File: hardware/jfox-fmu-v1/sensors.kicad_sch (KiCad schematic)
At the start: 5 parts, among them U1 ICM-42688-P, U2 ICM-45686, U3 BMI088, U4 BMP388, U5 FM25V02A

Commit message: Footprint every part, and verify each one exists
58 of 58 components now carry a footprint chosen against the package its
datasheet specifies, and check_fmu_footprints.py confirms every name resolves
to a file on disk.

Three of the names this design was carrying did not. The symbol library named
`Sensor_Motion:InvenSense_QFN-14_3x3mm_P0.5mm` and
`Sensor_Pressure:Bosch_LGA-10_2x2mm_P0.35mm`, neither of which is a footprint
in any installed library - both plausible, both fiction. The third was worse:
`Package_LGA:Bosch_LGA-14_3x2.5mm_P0.5mm` is real, matches the InvenSense
package on every word of its name, and is drawn for the BMI160 with 0.675 mm
pads where InvenSense wants 0.475 mm.

Notable choices, each traceable:
  LTC4417CGN  GN is the 16-lead narrow SSOP.
  TPS62132    RGT 3x3 VQFN. TI's land drawing (4222419/E) gives the exposed
              pad as 1.55 mm; KiCad's 1.6 mm variant is closest. Thermal-via
              variant, since the datasheet is explicit that the pad must be
              soldered and that dissipation limits output power.
  Bulk caps   4u7/10u/22u get an 0805, not the 0402 every other capacitor
              gets. Assigning one size to all of them produces a board that
              cannot be built from the BOM it ships with.
  L1          a generic 1210 land, and labelled as such - the 2.2 uH part is
              not chosen yet, since saturation current and DCR still have to
              be picked against the real 550 mA peak.

The checker was wrong on its first run, in a way worth recording because the
failure mode is self-concealing. It matched ref, value and footprint in one
regex with the footprint group optional, so a component with no footprint -
precisely what it exists to find - failed to match at all, dropped out of the
list, and the run reported "every component maps to a footprint" while the
count quietly fell by one. A check whose failure mode is to stop seeing the
failure is worse than no check. Now it splits into per-com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
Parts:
- U1, U2: footprint (none) -> jfox-fmu:InvenSense_LGA-14_2.5x3mm_P0.5mm
- U3: footprint (none) -> Package_LGA:Bosch_LGA-16_4.5x3mm_P0.5mm_LayoutBorder7x1y_ClockwisePinNumbering
- U4: footprint (none) -> jfox-fmu:Bosch_LGA-10_2x2mm_P0.5mm_LayoutBorder2x3y
- U5: footprint (none) -> Package_SO:SOIC-8_3.9x4.9mm_P1.27mm
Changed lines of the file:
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@@
+		)
+		)
+		(property "Footprint" "jfox-fmu:InvenSense_LGA-14_2.5x3mm_P0.5mm"
+			(at 66.04 59.69 0)
+			(hide yes)
+			(effects
+			(font
+				(size 1.27 1.27)
+			)
 		)
 		)
 		(instances
 			(project "jfox-fmu"
-				(path "/3f1d7739-de78-4a9b-8f02-2fa580b1af15"
+				(path "/fce3b1be-4717-4f75-b07b-c3376dbd2263"
 					(reference "U1")
 					(unit 1)
@@
 		)
 		)
+		(property "Footprint" "jfox-fmu:InvenSense_LGA-14_2.5x3mm_P0.5mm"
+			(at 154.94 59.69 0)
+			(hide yes)
+			(effects
+			(font
+				(size 1.27 1.27)
+			)
+		)
+		)
 		(instances
 			(project "jfox-fmu"
-				(path "/3f1d7739-de78-4a9b-8f02-2fa580b1af15"
+				(path "/fce3b1be-4717-4f75-b07b-c3376dbd2263"
 					(reference "U2")
 					(unit 1)
@@
 		)
 		)
+		(property "Footprint" "jfox-fmu:Bosch_LGA-10_2x2mm_P0.5mm_LayoutBorder2x3y"
+			(at 66.04 125.73 0)
+			(hide yes)
+			(effects
+			(font
+				(size 1.27 1.27)
+			)
+		)
+		)
 		(instances
 			(project "jfox-fmu"
-				(path "/3f1d7739-de78-4a9b-8f02-2fa580b1af15"
+				(path "/fce3b1be-4717-4f75-b07b-c3376dbd2263"
 					(reference "U4")
 					(unit 1)
@@
 		)
 		)
+		(property "Footprint" "Package_SO:SOIC-8_3.9x4.9mm_P1.27mm"
+			(at 154.94 125.73 0)
+			(hide yes)
+			(effects
+			(font
+				(size 1.27 1.27)
+			)
+		)
+		)
 		(instances
 			(project "jfox-fmu"
-				(path "/3f1d7739-de78-4a9b-8f02-2fa580b1af15"
+				(path "/fce3b1be-4717-4f75-b07b-c3376dbd2263"
 					(reference "U5")
 					(unit 1)
@@
 		)
 		)
+		(property "Footprint" "Package_LGA:Bosch_LGA-16_4.5x3mm_P0.5mm_LayoutBorder7x1y_ClockwisePinNumbering"
+			(at 66.04 191.77 0)
+			(hide yes)
+			(effects
+			(font
+				(size 1.27 1.27)
+			)
+		)
+		)
 		(instances
 			(project "jfox-fmu"
-				(path "/3f1d7739-de78-4a9b-8f02-2fa580b1af15"
+				(path "/fce3b1be-4717-4f75-b07b-c3376dbd2263"
 					(reference "U3")
 					(unit 1)

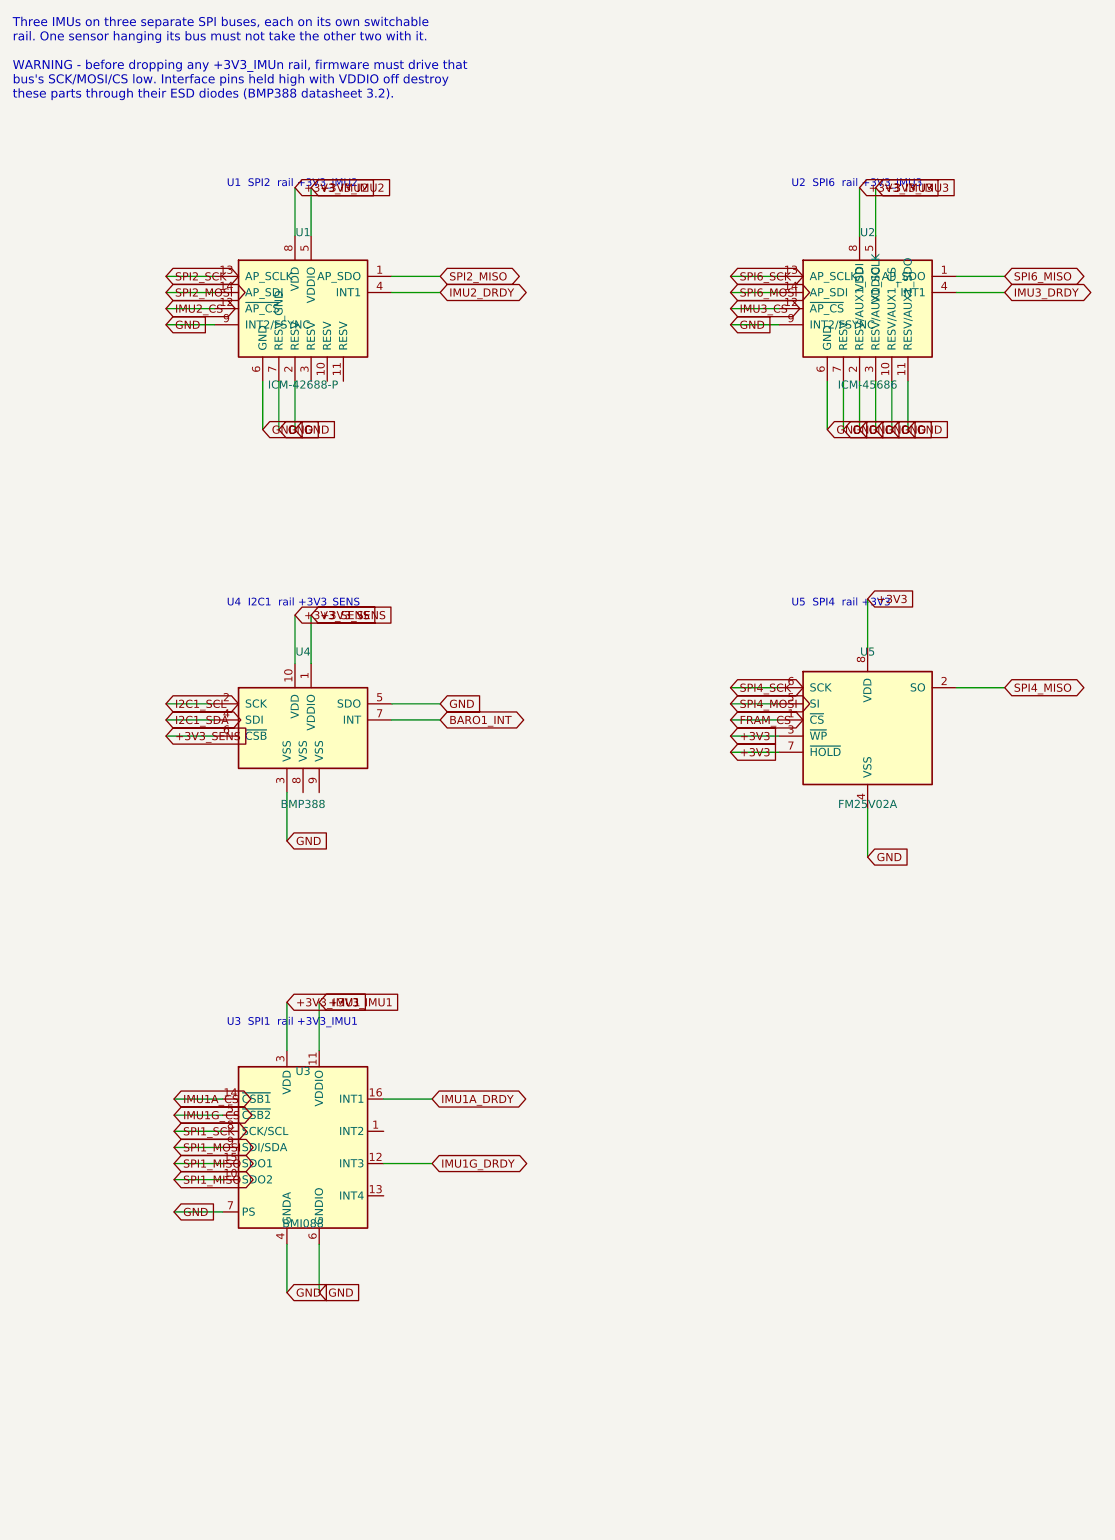
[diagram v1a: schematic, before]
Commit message: Add the two sensors the design said it had
ARCHITECTURE.md specifies two barometers from two vendors and an internal
magnetometer. The schematic had one barometer and no magnetometer, and had had
neither for the whole life of the board. Every check passed the entire time.

That is the interesting part. The datasheet checks ask "is this part wired the
way its datasheet says", and all of them can pass on a board that is wired
perfectly and is still the wrong board. The nets for the missing sensors
existed - MAG_DRDY and BARO2_INT, correctly named, allocated to real MCU pins,
going nowhere - and "isolated label" is such ordinary ERC noise that sixty of
them hid two absent sensors.

U7 ICP-20100 (TDK) and U6 BMM150 (Bosch), both on I2C1, both from the
datasheets rather than from memory:

  ICP-20100  DS-000416 rev 1.3. Pinout table 18, strapping from figure 10's
             I2C typical circuit: CSB to VDDIO selects I2C, AD0 low gives
             0x63, pins 8 and 9 are "Connect to Ground" and are typed
             power_in so ERC objects if they float.
  BMM150     BST-BMM150-DS001-05 rev 1.4 table 32 and section 4.1: PS to
             VDDIO for reliable protocol selection, CSB and SDO both low for
             the default 0x10.

Addresses checked against each other rather than assumed: 0x10, 0x63, 0x76.
No collision on the shared bus.

R4/R5 4k7 pull-ups on I2C1. Both datasheets state outright that the bus needs
them; without them the line never releases and no sensor on it answers. The
board has had an I2C bus with no pull-ups since the day it was drawn.

The ICP-20100 footprint had to be drawn. It is the same 2x2 mm body and the
same ten pins as the BMP388 and a completely different land - Bosch puts three
pads left and right, TDK puts three top and bottom. Reusing the BMP388 land
would have placed ten pads that all landed somewhere and none on a terminal.

And the check that would have caught this in the first place:
check_fmu_objective.py encodes ARCHITECTURE.md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
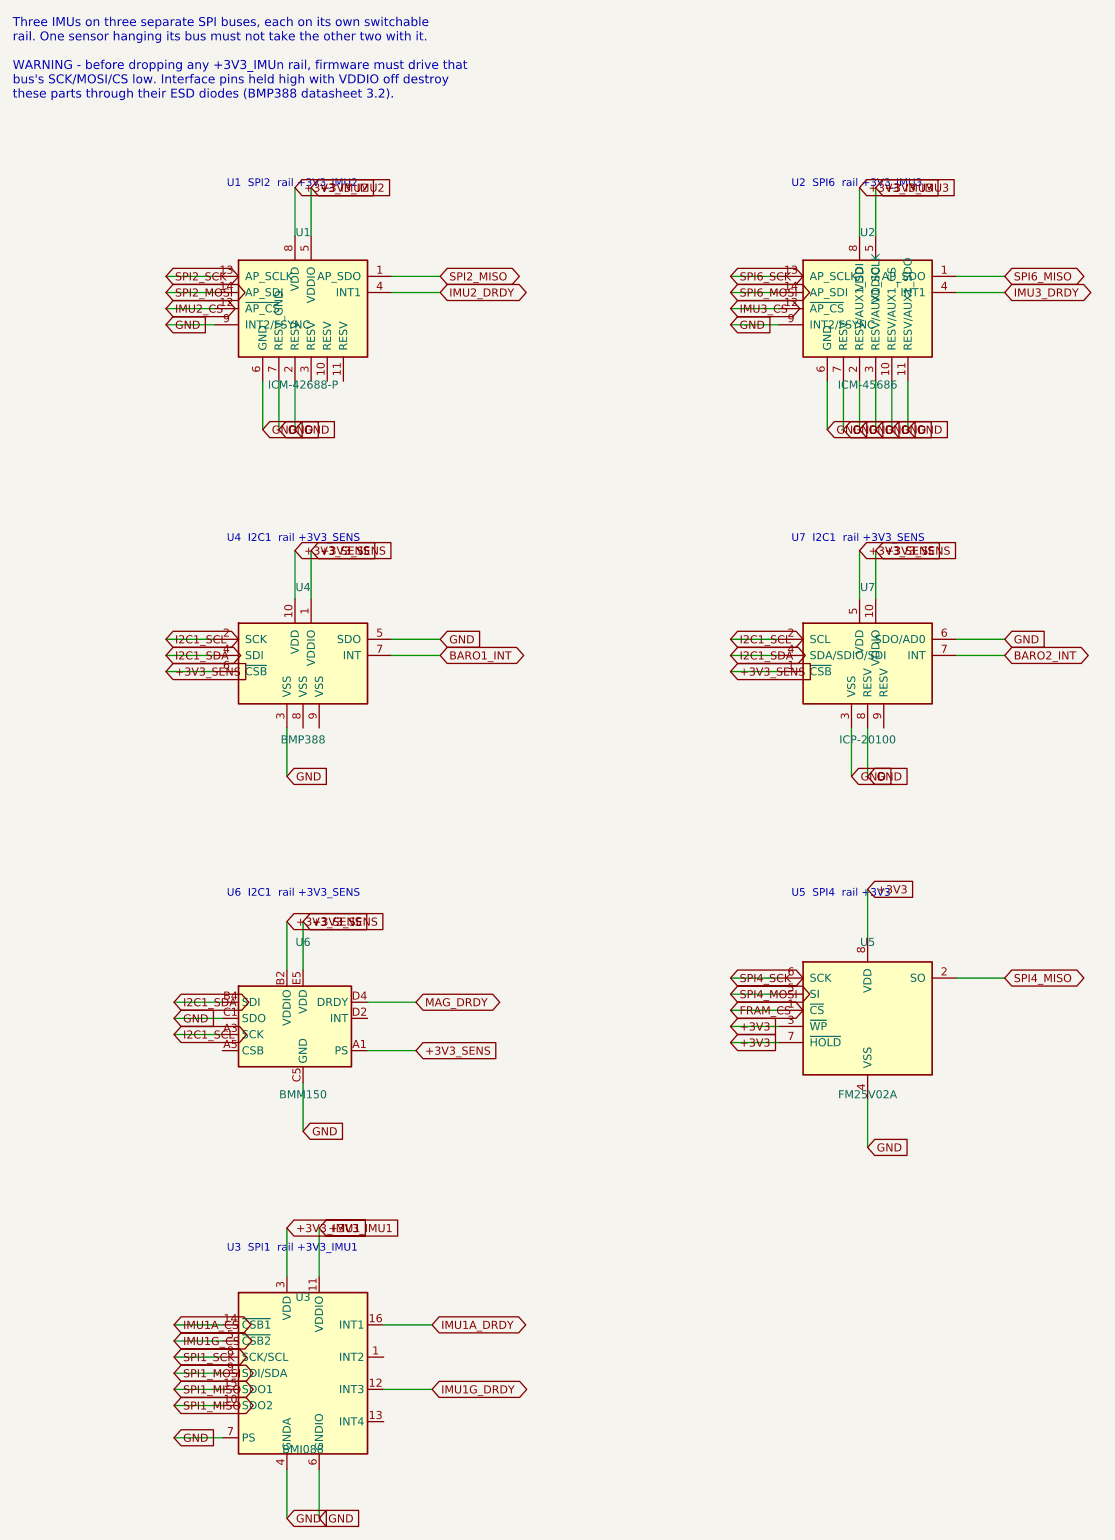
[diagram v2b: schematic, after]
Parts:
- added U6: BMM150, Package_CSP:WLCSP-12_1.56x1.56mm_P0.4mm, symbol Sensor_Magnetic:BMM150
- added U7: ICP-20100, jfox-fmu:InvenSense_LGA-10_2x2mm_P0.5mm, symbol jfox-fmu:ICP-20100
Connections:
- net +3V3_SENS: now also U6.A1 (PS), U6.B2 (VDDIO), U6.E5 (VDD), U7.1 (~{CSB}), U7.10 (VDDIO), U7.5 (VDD)
- net GND: now also U6.C1 (SDO), U6.C5 (GND), U6.E1 (GND), U6.E3 (GND), U7.3 (VSS), U7.6 (SDO/AD0), U7.8 (RESV)
- net I2C1_SCL: now also U6.A3 (SCK), U7.2 (SCL)
- net I2C1_SDA: now also U6.B4 (SDI), U7.4 (SDA/SDIO/SDI)
- new net BARO2_INT: U7.7 (INT)
- new net MAG_DRDY: U6.D4 (DRDY)
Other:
- note added: "U6 I2C1 rail +3V3_SENS"
- note added: "U7 I2C1 rail +3V3_SENS"
